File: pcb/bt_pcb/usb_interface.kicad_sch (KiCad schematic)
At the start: 8 parts, among them J6 UJ32-C-H-G-SMT-TR-68

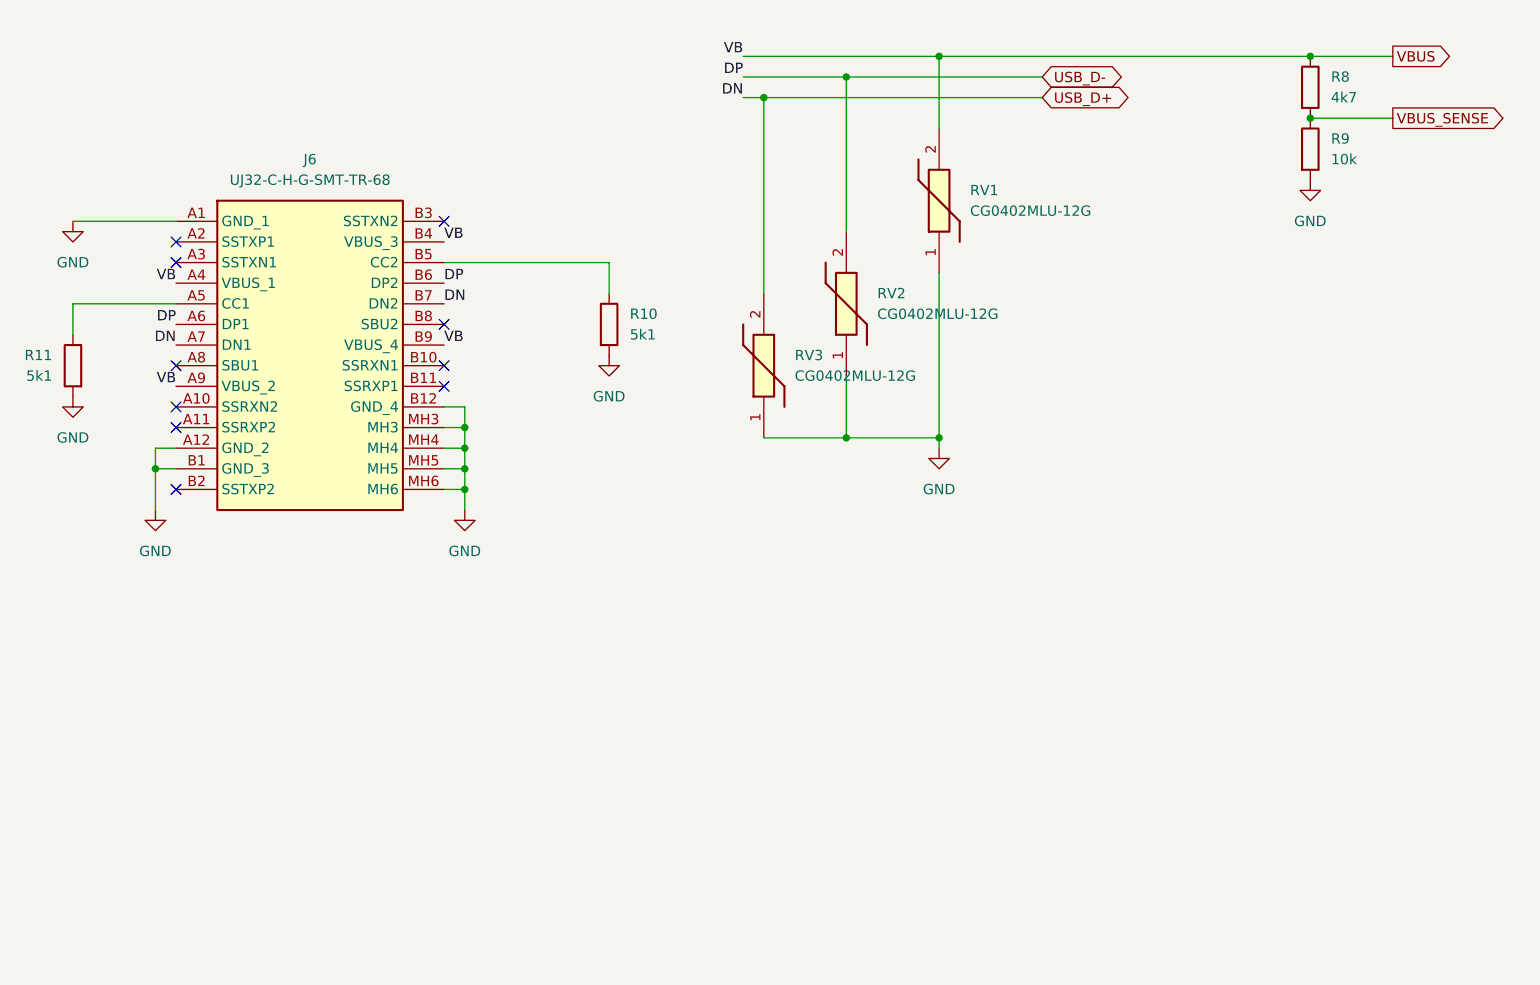
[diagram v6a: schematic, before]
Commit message: pcb with some schematic tuning
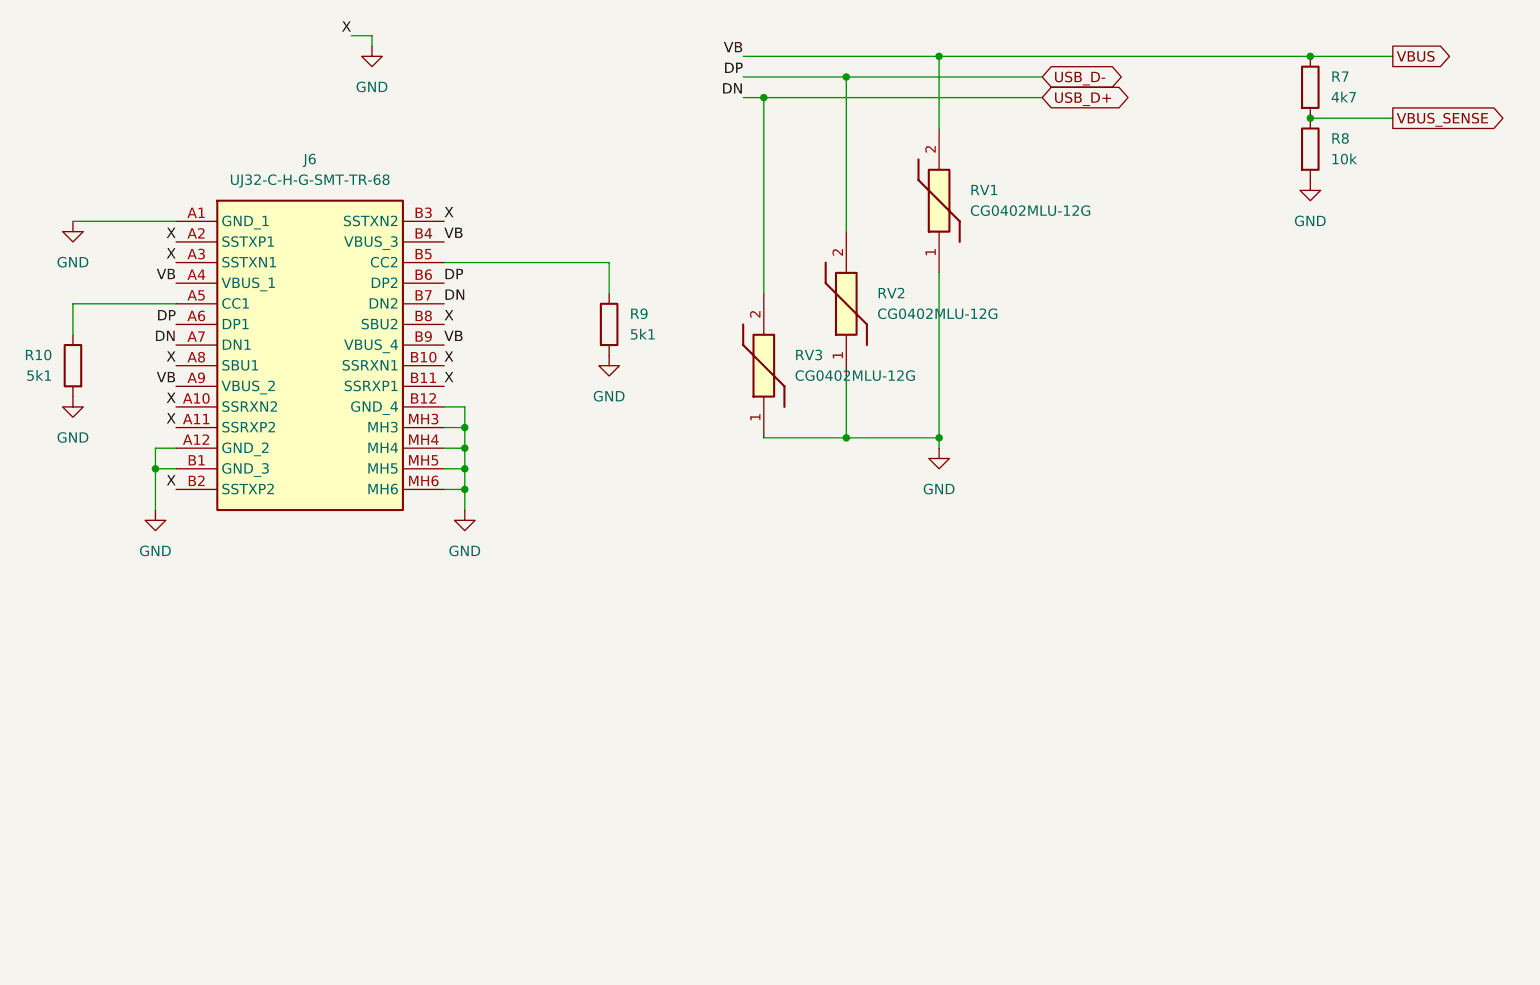
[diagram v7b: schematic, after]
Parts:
- renumbered R11 to R10, R8 to R7, R9 to R8, R10 to R9
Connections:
- net GND: now also J6.A10 (SSRXN2), J6.A11 (SSRXP2), J6.A2 (SSTXP1), J6.A3 (SSTXN1), J6.A8 (SBU1), J6.B10 (SSRXN1), J6.B11 (SSRXP1), J6.B2 (SSTXP2), J6.B3 (SSTXN2), J6.B8 (SBU2)
- no-connect marks 10 -> 0
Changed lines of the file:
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@@
 		(color 0 0 0 0)
 	)
-	(no_connect
-		(at 91.44 72.39)
-	)
-	(no_connect
-		(at 91.44 92.71)
-	)
-	(no_connect
-		(at 124.46 69.85)
-	)
-	(no_connect
-		(at 91.44 95.25)
-	)
-	(no_connect
-		(at 124.46 90.17)
-	)
-	(no_connect
-		(at 91.44 74.93)
-	)
-	(no_connect
-		(at 124.46 82.55)
-	)
-	(no_connect
-		(at 91.44 102.87)
-	)
-	(no_connect
-		(at 124.46 87.63)
-	)
-	(no_connect
-		(at 91.44 87.63)
-	)
 	(wire
 		(pts
@@
 	(wire
 		(pts
+			(xy 115.57 46.99) (xy 115.57 48.26)
+		)
+		(stroke
+			(width 0)
+			(type default)
+		)
+	)
+	(wire
+		(pts
+			(xy 113.03 46.99) (xy 115.57 46.99)
+		)
+		(stroke
+			(width 0)
+			(type default)
+		)
+	)
+	(wire
+		(pts
 			(xy 127 97.79) (xy 124.46 97.79)
 		)
@@
 			(width 0)
 			(type default)
+		)
+	)
+	(label "X"
+		(at 91.44 74.93 180)
+		(effects
+			(font
+				(size 1.27 1.27)
+			)
+			(justify right bottom)
+		)
+	)
+	(label "X"
+		(at 91.44 92.71 180)
+		(effects
+			(font
+				(size 1.27 1.27)
+			)
+			(justify right bottom)
+		)
+	)
+	(label "X"
+		(at 124.46 69.85 0)
+		(effects
+			(font
+				(size 1.27 1.27)
+			)
+			(justify left bottom)
+		)
+	)
+	(label "X"
+		(at 124.46 87.63 0)
+		(effects
+			(font
+				(size 1.27 1.27)
+			)
+			(justify left bottom)
+		)
+	)
+	(label "X"
+		(at 124.46 82.55 0)
+		(effects
+			(font
+				(size 1.27 1.27)
+			)
+			(justify left bottom)
 		)
 	)
@@
 		)
 	)
+	(label "X"
+		(at 91.44 87.63 180)
+		(effects
+			(font
+				(size 1.27 1.27)
+			)
+			(justify right bottom)
+		)
+	)
+	(label "X"
+		(at 91.44 72.39 180)
+		(effects
+			(font
+				(size 1.27 1.27)
+			)
+			(justify right bottom)
+		)
+	)
 	(label "DP"
 		(at 91.44 82.55 180)
@@
 		)
 	)
+	(label "X"
+		(at 124.46 90.17 0)
+		(effects
+			(font
+				(size 1.27 1.27)
+			)
+			(justify left bottom)
+		)
+	)
 	(label "VB"
 		(at 91.44 90.17 180)
@@
 		)
 	)
+	(label "X"
+		(at 91.44 102.87 180)
+		(effects
+			(font
+				(size 1.27 1.27)
+			)
+			(justify right bottom)
+		)
+	)
+	(label "X"
+		(at 91.44 95.25 180)
+		(effects
+			(font
+				(size 1.27 1.27)
+			)
+			(justify right bottom)
+		)
+	)
 	(label "VB"
 		(at 161.29 49.53 180)
+		(effects
+			(font
+				(size 1.27 1.27)
+			)
+			(justify right bottom)
+		)
+	)
+	(label "X"
+		(at 113.03 46.99 180)
 		(effects
 			(font
@@
 		(on_board yes)
 		(dnp no)
-		(property "Reference" "R11"
+		(property "Reference" "R10"
 			(at 76.2 86.36 0)
 			(effects
@@
 			(project "bt_pcb"
 				(path "/eb787481-08cd-41a4-a128-173fa6227c32/81f44120-5006-4955-ab2c-f15dbf34b899"
-					(reference "R11")
+					(reference "R10")
 					(unit 1)
 				)
@@
 		(dnp no)
 		(fields_autoplaced yes)
-		(property "Reference" "#PWR029"
+		(property "Reference" "#PWR035"
 			(at 185.42 104.14 0)
 			(effects
@@
 			(project "bt_pcb"
 				(path "/eb787481-08cd-41a4-a128-173fa6227c32/81f44120-5006-4955-ab2c-f15dbf34b899"
-					(reference "#PWR029")
+					(reference "#PWR035")
 					(unit 1)
 				)
@@
 		(dnp no)
 		(fields_autoplaced yes)
-		(property "Reference" "#PWR030"
+		(property "Reference" "#PWR036"
 			(at 88.9 111.76 0)
 			(effects
@@
 			(project "bt_pcb"
 				(path "/eb787481-08cd-41a4-a128-173fa6227c32/81f44120-5006-4955-ab2c-f15dbf34b899"
-					(reference "#PWR030")
+					(reference "#PWR036")
 					(unit 1)
 				)
@@
 		(dnp no)
 		(fields_autoplaced yes)
-		(property "Reference" "#PWR025"
+		(property "Reference" "#PWR031"
 			(at 231.14 71.12 0)
 			(effects
@@
 			(project "bt_pcb"
 				(path "/eb787481-08cd-41a4-a128-173fa6227c32/81f44120-5006-4955-ab2c-f15dbf34b899"
-					(reference "#PWR025")
+					(reference "#PWR031")
 					(unit 1)
 				)
@@
 		(dnp no)
 		(fields_autoplaced yes)
-		(property "Reference" "#PWR027"
+		(property "Reference" "#PWR033"
 			(at 144.78 92.71 0)
 			(effects
@@
 			(project "bt_pcb"
 				(path "/eb787481-08cd-41a4-a128-173fa6227c32/81f44120-5006-4955-ab2c-f15dbf34b899"
-					(reference "#PWR027")
+					(reference "#PWR033")
 					(unit 1)
 				)
@@
 		(dnp no)
 		(fields_autoplaced yes)
-		(property "Reference" "R8"
+		(property "Reference" "R7"
 			(at 233.68 52.07 0)
 			(effects
@@
 			(project "bt_pcb"
 				(path "/eb787481-08cd-41a4-a128-173fa6227c32/81f44120-5006-4955-ab2c-f15dbf34b899"
-					(reference "R8")
+					(reference "R7")
 					(unit 1)
 				)
@@
 		(dnp no)
 		(fields_autoplaced yes)
-		(property "Reference" "#PWR031"
+		(property "Reference" "#PWR037"
 			(at 127 111.76 0)
 			(effects
@@
 			(project "bt_pcb"
 				(path "/eb787481-08cd-41a4-a128-173fa6227c32/81f44120-5006-4955-ab2c-f15dbf34b899"
-					(reference "#PWR031")
+					(reference "#PWR037")
 					(unit 1)
 				)
@@
 		(dnp no)
 		(fields_autoplaced yes)
-		(property "Reference" "R9"
+		(property "Reference" "R8"
 			(at 233.68 59.69 0)
 			(effects
@@
 			(project "bt_pcb"
 				(path "/eb787481-08cd-41a4-a128-173fa6227c32/81f44120-5006-4955-ab2c-f15dbf34b899"
-					(reference "R9")
+					(reference "R8")
 					(unit 1)
 				)
@@
 		(dnp no)
 		(fields_autoplaced yes)
-		(property "Reference" "#PWR028"
+		(property "Reference" "#PWR034"
 			(at 78.74 97.79 0)
 			(effects
@@
 			(project "bt_pcb"
 				(path "/eb787481-08cd-41a4-a128-173fa6227c32/81f44120-5006-4955-ab2c-f15dbf34b899"
-					(reference "#PWR028")
+					(reference "#PWR034")
 					(unit 1)
 				)
@@
 		(dnp no)
 		(fields_autoplaced yes)
-		(property "Reference" "#PWR026"
+		(property "Reference" "#PWR032"
 			(at 78.74 76.2 0)
 			(effects
@@
 			(project "bt_pcb"
 				(path "/eb787481-08cd-41a4-a128-173fa6227c32/81f44120-5006-4955-ab2c-f15dbf34b899"
-					(reference "#PWR026")
+					(reference "#PWR032")
+					(unit 1)
+				)
+			)
+		)
+	)
+	(symbol
+		(lib_name "GND_1")
+		(lib_id "power:GND")
+		(at 115.57 48.26 0)
+		(unit 1)
+		(exclude_from_sim no)
+		(in_bom yes)
+		(on_board yes)
+		(dnp no)
+		(fields_autoplaced yes)
+		(property "Reference" "#PWR0152"
+			(at 115.57 54.61 0)
+			(effects
+				(font
+					(size 1.27 1.27)
+				)
+				(hide yes)
+			)
+		)
+		(property "Value" "GND"
+			(at 115.57 53.34 0)
+			(effects
+				(font
+					(size 1.27 1.27)
+				)
+			)
+		)
+		(property "Footprint" ""
+			(at 115.57 48.26 0)
+			(effects
+				(font
+					(size 1.27 1.27)
+				)
+				(hide yes)
+			)
+		)
+		(property "Datasheet" ""
+			(at 115.57 48.26 0)
+			(effects
+				(font
+					(size 1.27 1.27)
+				)
+				(hide yes)
+			)
+		)
+		(property "Description" "Power symbol creates a global label with name \"GND\" , ground"
+			(at 115.57 48.26 0)
+			(effects
+				(font
+					(size 1.27 1.27)
+				)
+				(hide yes)
+			)
+		)
+		(pin "1"
+		)
+		(instances
+			(project "bt_pcb"
+				(path "/eb787481-08cd-41a4-a128-173fa6227c32/81f44120-5006-4955-ab2c-f15dbf34b899"
+					(reference "#PWR0152")
 					(unit 1)
 				)
@@
 		(dnp no)
 		(fields_autoplaced yes)
-		(property "Reference" "R10"
+		(property "Reference" "R9"
 			(at 147.32 81.28 0)
 			(effects
@@
 			(project "bt_pcb"
 				(path "/eb787481-08cd-41a4-a128-173fa6227c32/81f44120-5006-4955-ab2c-f15dbf34b899"
-					(reference "R10")
+					(reference "R9")
 					(unit 1)
 				)
